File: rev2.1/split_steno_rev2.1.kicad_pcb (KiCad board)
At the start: 2 copper layers, 71 parts, among them J1 Audio-Jack-4, J2 USB_OTG, P1 TC2030-IDC, SW1 SW_Push, SW10 SW_Push, SW11 SW_Push, SW12 SW_Push, SW13 SW_Push, SW14 SW_Push, SW15 SW_Push, SW16 SW_Push, SW17 SW_Push, SW18 SW_Push, SW19 SW_Push, SW2 SW_Push, SW20 SW_Push, SW21 SW_Push, SW22 Switch-6P-2S2T, SW3 SW_Push, SW4 SW_Push, SW5 SW_Push, SW6 SW_Push, SW7 SW_Push, SW8 SW_Push, SW9 SW_Push, U1 74LVC1G34, U2 MCP73831, U3 MCP1700, U4 MCP1700, U5 ATXMEGA128A4U-AU, U6 nRF24L01_module

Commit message: laid out pcb
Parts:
- removed the LED4 at (138.1, 114.3)
- removed R9: 4.7k, Resistors_SMD:R_0603_HandSoldering
- removed the REF** at (116.7, 121.4)
- removed the REF** at (40.5, 121.4)
- removed the REF** at (135.7, 58.8)
- removed the REF** at (40.5, 64.3)
- C1: value 4.7uF -> 0.1uF
- C5: value 0.1uF -> 4.7uF
- J1: value Audio-Jack-4 -> USB_OTG; footprint Keebio-Parts:TRRS-PJ-320A -> keyboard_parts:USB_miniB; moved to B.Cu
- J2: value USB_OTG -> Audio-Jack-4; footprint keyboard_parts:USB_miniB -> Keebio-Parts:TRRS-PJ-320A; moved to F.Cu
- R8: value 100k -> 4.7k
- SW13: footprint Keebio-Parts:Hybrid_PCB_100H_Dual_hole -> Keebio-Parts:Hybrid_PCB_100H_Dual_hole-flip
- moved C1 139.0 mm to (47.4, 123.0)
- moved C4 77.2 mm to (114.7, 119.7)
- moved C11 66.9 mm to (69.2, 120.1)
- moved C12 66.8 mm to (67.0, 130.4)
- moved C10 66.8 mm to (79.5, 131.5)
- moved U5 66.7 mm to (73.8, 126.3)
- moved C9 66.7 mm to (80.8, 122.3)
- moved LED3 59.4 mm to (88.5, 71.5)
- moved J2 58.3 mm to (108.1, 61.6)
- moved LED2 56.6 mm to (50.4, 70.1)
- moved J1 50.4 mm to (59.5, 65.4)
- moved LED1 47.7 mm to (50.0, 116.8)
- moved C2 45.5 mm to (50.1, 78.6)
- moved C3 42.7 mm to (87.9, 80.5)
- moved C5 9.74 mm to (56.0, 55.2)
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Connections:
- J1 pad 1: +3V3 -> Net-(F1-Pad1)
- J1 pad 2: /SCL -> /D-
- J1 pad 3: /SDA -> /D+
- J1 pad 4: GND -> Net-(J1-Pad4)
- J2 pad 1: Net-(F1-Pad1) -> +3V3
- J2 pad 2: /D- -> /SCL
- J2 pad 3: /D+ -> /SDA
- J2 pad 4: Net-(J2-Pad4) -> GND
- R8 pad 1: Net-(J2-Pad4) -> +3V3
- R8 pad 2: GND -> /SCL
- U5 pad 23: /KEY8 -> /KEY13
- U5 pad 42: /KEY13 -> /KEY8
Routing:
- net VCC: track 8.66 -> 0.00 mm
- net GND: track 8.65 -> 0.00 mm

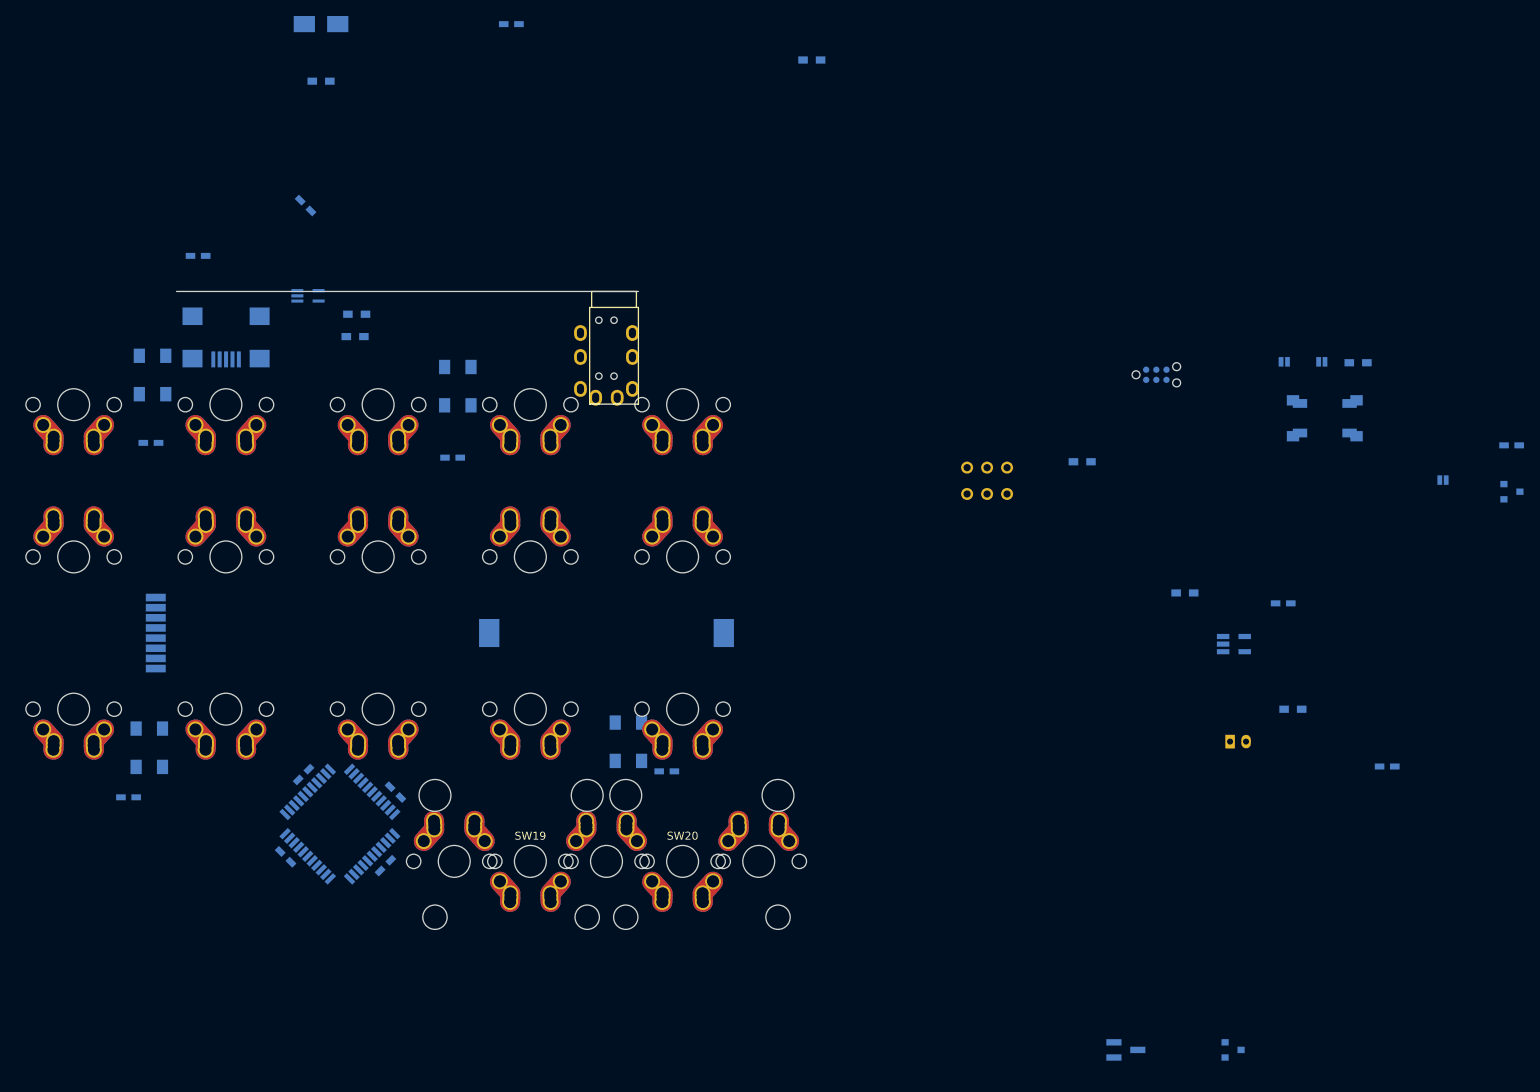
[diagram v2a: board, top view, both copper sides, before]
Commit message: added 2 more ws2812b
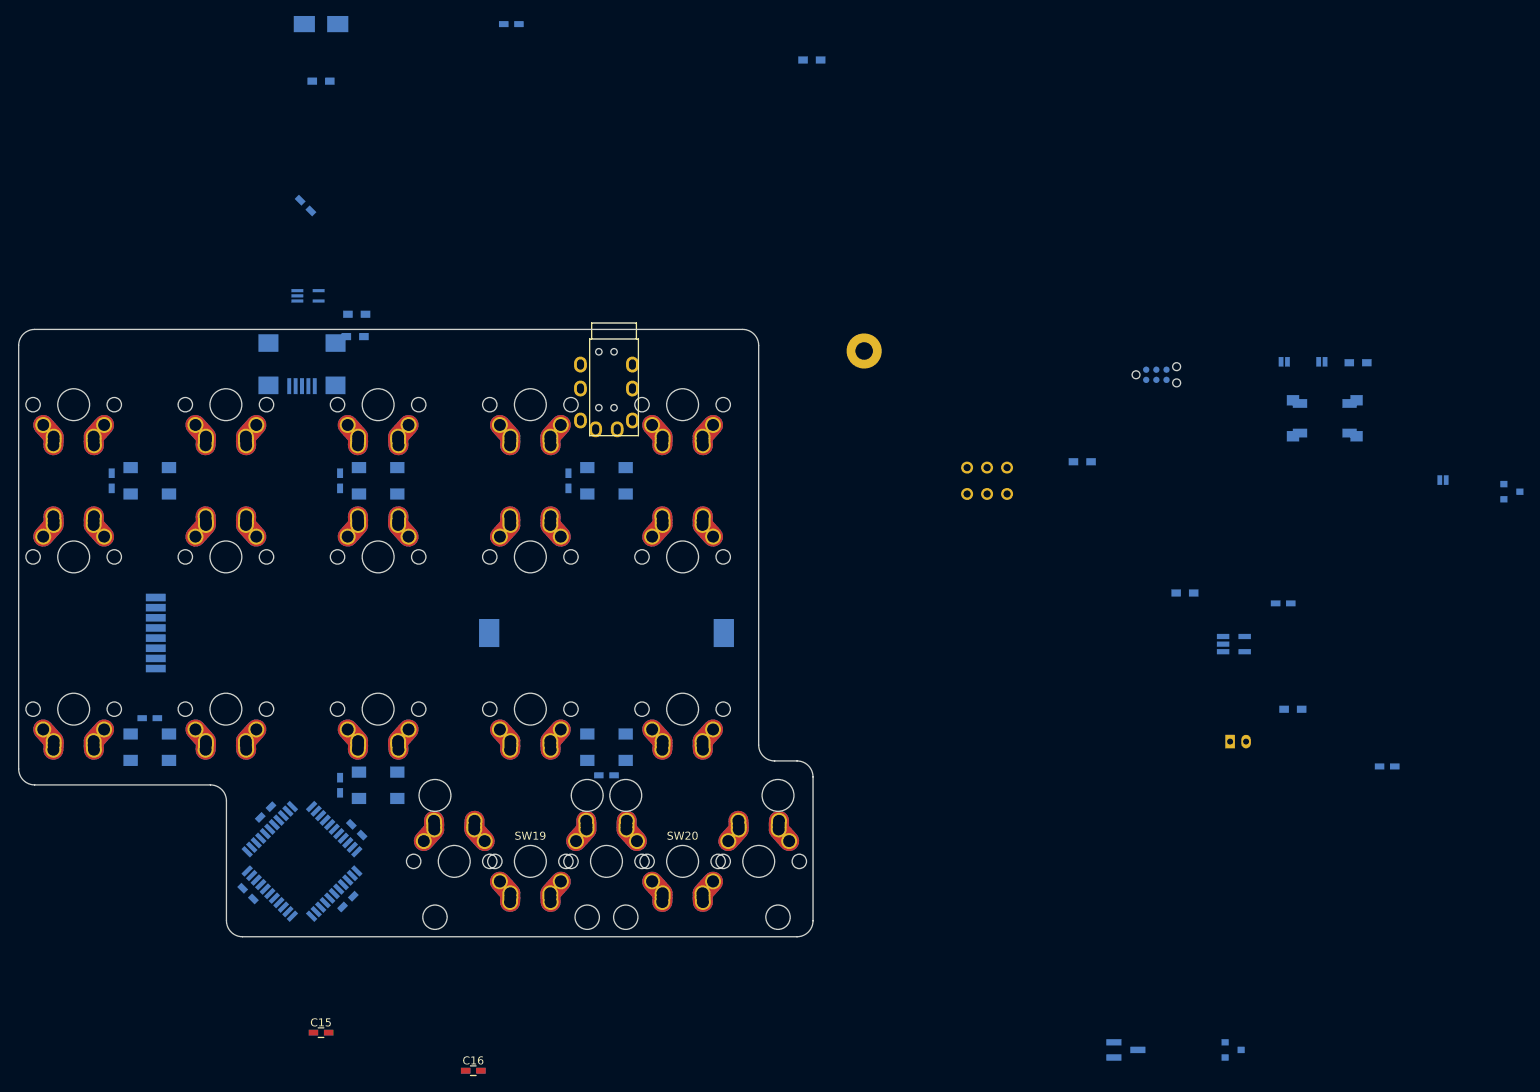
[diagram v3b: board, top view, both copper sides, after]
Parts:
- added ?: , Mounting_Holes:MountingHole_2.2mm_M2_Pad, F.Cu at (139.4, 67.1)
- added C15: 4.7uF, Capacitors_SMD:C_0603_HandSoldering, F.Cu at (71.4, 152.4)
- added C16: 4.7uF, Capacitors_SMD:C_0603_HandSoldering, F.Cu at (90.5, 157.2)
- added G***: LOGO, airi_logo:airi_icon-7.6, B.Cu at (69.1, 131.0)
- added LED5: WS2812B, WS2812B:WS2812B, B.Cu at (107.2, 116.7)
- added LED6: WS2812B, WS2812B:WS2812B, B.Cu at (78.6, 121.4)
- C5, C6: value 4.7uF -> 0.1uF
- moved C6 152.6 mm to (73.8, 121.4), turned to 270 degrees
- moved C5 82.7 mm to (107.2, 120.2), turned to 180 degrees
- moved C4 38.4 mm to (102.4, 83.3), turned to 270 degrees
- moved LED4 32.8 mm to (107.2, 83.3), turned to 90 degrees
- moved LED3 15.5 mm to (78.6, 83.3), turned to 90 degrees
- moved C3 14.4 mm to (73.8, 83.3), turned to 270 degrees
- moved LED2 13.2 mm to (50.0, 83.3), turned to 90 degrees
- moved C1 10.2 mm to (50.0, 113.0), turned to 180 degrees
- moved J1 10.1 mm to (69.0, 68.8)
- moved C2 6.82 mm to (45.2, 83.3), turned to 270 degrees
- moved C9 6.75 mm to (75.9, 127.0)
- moved C11 6.68 mm to (64.5, 124.8)
- moved U5 6.66 mm to (69.1, 131.0)
- moved C12 6.58 mm to (62.3, 135.0)
- moved C10 6.51 mm to (74.8, 136.0)
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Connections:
- C6 pad 1: /BAT_LI_ION -> +5V
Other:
- board outline added: 99.4 x 76 mm

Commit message: finished mounting hole placement
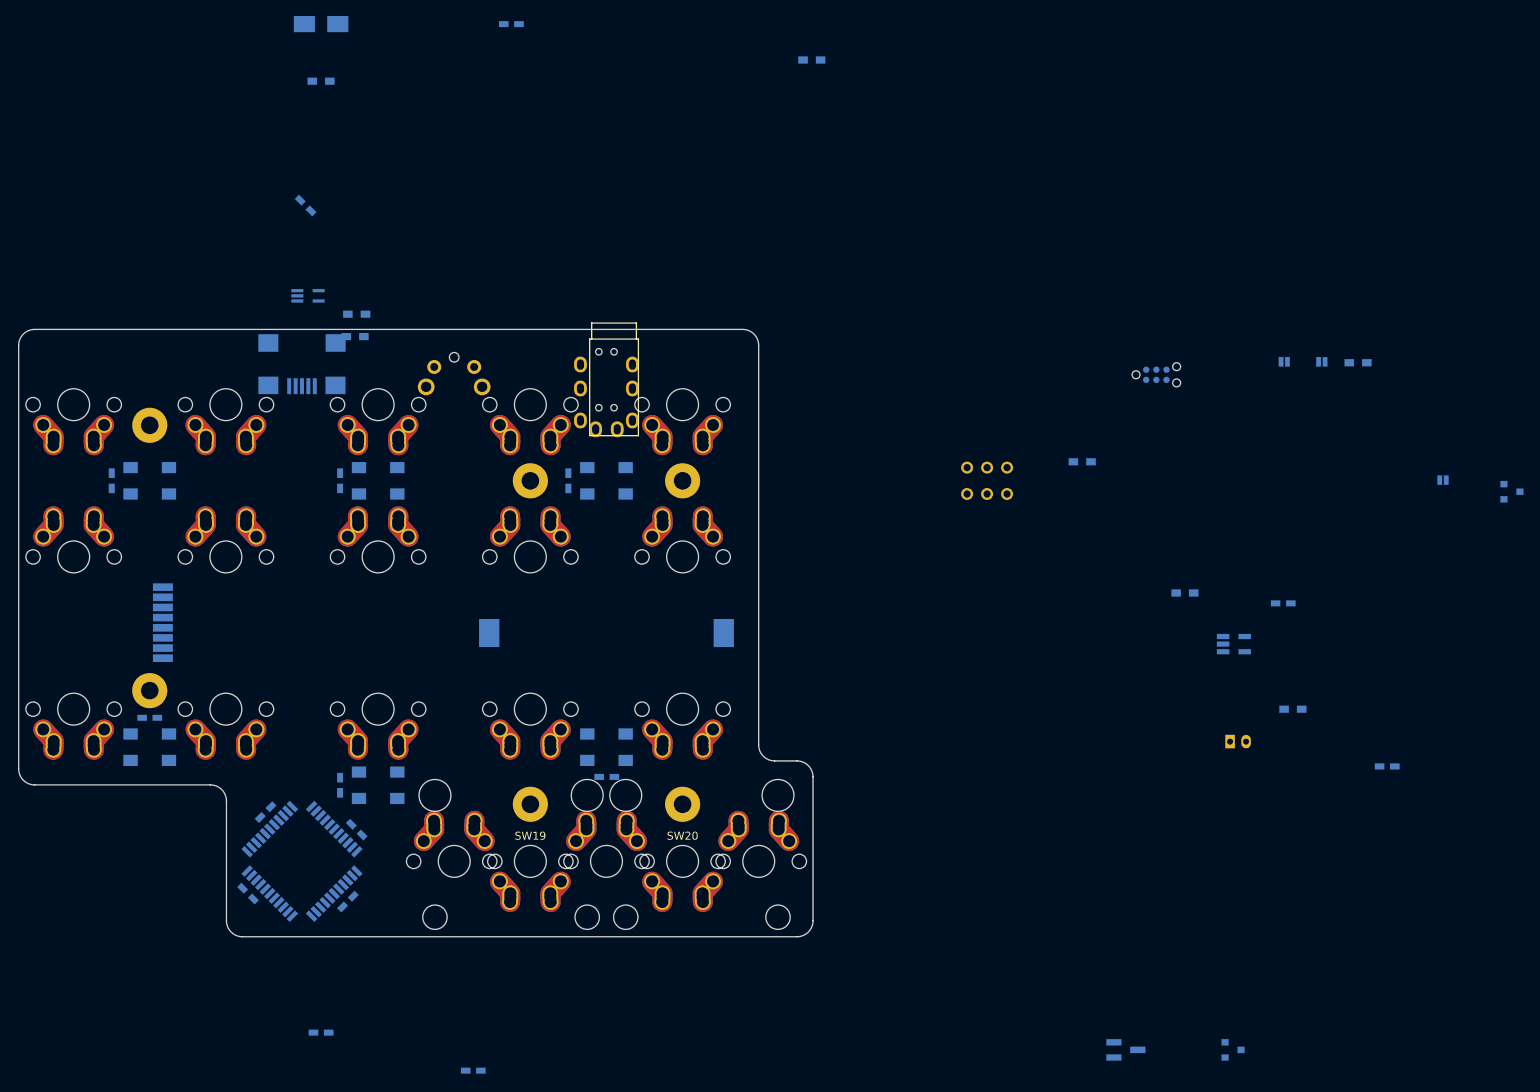
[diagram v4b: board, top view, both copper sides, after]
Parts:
- added ?: , Mounting_Holes:MountingHole_2.2mm_M2_Pad, F.Cu at (50.0, 76.4)
- added ?: , Mounting_Holes:MountingHole_2.2mm_M2_Pad, F.Cu at (50.0, 109.6)
- added ?: , Mounting_Holes:MountingHole_2.2mm_M2_Pad, F.Cu at (97.6, 123.8)
- added ?: , Mounting_Holes:MountingHole_2.2mm_M2_Pad, F.Cu at (116.7, 83.3)
- added ?: , Mounting_Holes:MountingHole_2.2mm_M2_Pad, F.Cu at (97.6, 83.3)
- C15, C16: moved to B.Cu
- SW21: footprint switch:SwitchPush_C&K_MultiFoot_RS-187R05A2-DS_And_PTS645_SMT -> Keebio-Parts:SW_Tactile_SPST_Angled_MJTP1117
- moved SW21 106.6 mm to (90.6, 69.1), turned to 180 degrees
- moved ? 61.1 mm to (116.7, 123.8)
- moved U6 1.57 mm to (50.9, 101.1)
- moved C5 0.21 mm to (107.2, 120.4)

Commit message: updated some footprints
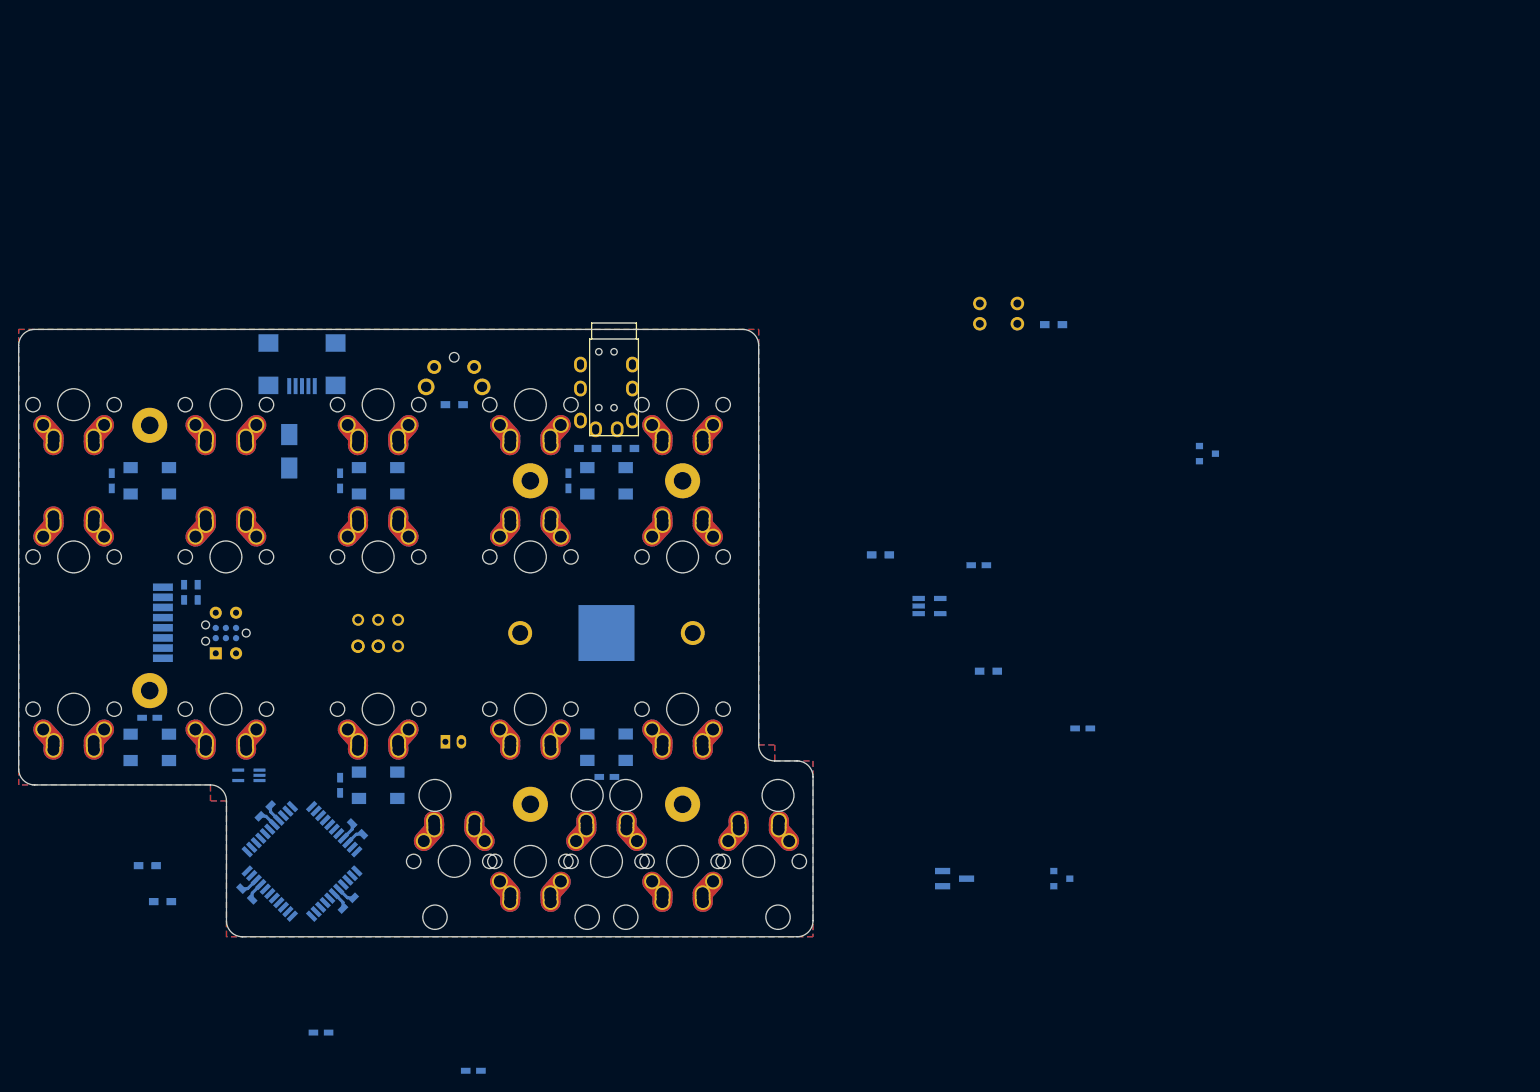
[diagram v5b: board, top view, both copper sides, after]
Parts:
- BT1: footprint Battery_Holders:Keystone_1058_1x2032-CoinCell -> battery:CR2032_BK-913
- JP1, JP2, JP3: footprint keyboard_parts:SOLDER_JUMPER_2 -> jumper:Jumper_1x02_P2.54mm_THT
- P1: footprint Connectors:Tag-Connect_TC2030-IDC-NL -> Tag-Connect:TC2030-NL_SMALL_AND_IDC_PDI_Extra_Pads
- SW15, SW16, SW5, SW6: footprint Keebio-Parts:Hybrid_PCB_100H_Dual_hole -> Keebio-Parts:Hybrid_PCB_100H_Dual_hole-flip
- moved JP2 134.8 mm to (78.6, 104.0), turned to 90 degrees
- moved P1 120.8 mm to (59.5, 102.4), turned to 180 degrees
- moved BT2 98.2 mm to (87.0, 116.0)
- moved C14 81.2 mm to (56.0, 97.3), turned to 270 degrees
- moved R6 78.9 mm to (88.1, 73.8), turned to 180 degrees
- moved SW22 78.5 mm to (78.6, 102.4)
- moved R4 77.4 mm to (51.6, 136.0)
- moved R5 71.1 mm to (49.7, 131.5)
- moved U1 60.5 mm to (62.4, 120.2), turned to 180 degrees
- moved R8 59.7 mm to (109.5, 79.3)
- moved R7 56.1 mm to (104.8, 79.3), turned to 180 degrees
- moved F1 53.6 mm to (67.5, 79.7), turned to 270 degrees
- moved C13 50.7 mm to (54.3, 97.3), turned to 270 degrees
- moved JP3 38.4 mm to (153.9, 63.7)
- moved R1 38.4 mm to (163.1, 63.8)
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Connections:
- REF** pad 1: (no net) -> +3V3
- REF** pad 2: (no net) -> /SCL
- REF** pad 3: (no net) -> /SDA
- REF** pad 4: (no net) -> GND
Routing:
- net VCC: track 0.00 -> 9.21 mm
- net GND: track 0.00 -> 9.17 mm
- added copper zone on B.Cu, net GND
- added copper zone on F.Cu, net GND
